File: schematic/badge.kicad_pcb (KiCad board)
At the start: 2 copper layers, 90.2 x 45.7 mm, 50 parts, among them J1 Left2, J10 Left1, J11 Penny2, J12 Penny1, J13 Penny0, J14 Power, J15 Right5, J2 Left3, J4 Serial, J5 Penny3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

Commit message: New board revision
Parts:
- removed LED1, LED10, LED2, LED3, LED4, LED5, LED6, LED7, LED8, LED9: WS2812B, LEDs:LED_WS2812B-PLCC4
- added REF***: OSHW-Logo_7.5x8mm_SilkScreen, Symbols:OSHW-Logo_7.5x8mm_SilkScreen, F.Cu at (96.9, 126.7)
- LS1: moved to B.Cu
- moved BT1 21.8 mm to (126.7, 117.6)
- moved J1 17.5 mm to (147.6, 102.2)
- moved J2 13.1 mm to (148.2, 106.4), turned to 180 degrees
- moved J14 12.7 mm to (88.2, 127.3)
- moved 1000 6.37 mm to (165.6, 107.9)
- moved 0110 6.37 mm to (121.4, 108.0)
- moved C6 6.37 mm to (119.4, 111.8)
- moved C7 6.37 mm to (110.5, 111.8)
- moved C8 6.37 mm to (101.6, 111.8)
- moved C9 6.37 mm to (92.7, 111.8)
- moved 0001 6.37 mm to (103.7, 108.0)
- moved 0010 6.37 mm to (139.2, 108.0)
- moved 0100 6.37 mm to (157.0, 108.0)
- moved 1001 6.37 mm to (94.8, 108.0)
- moved 1010 6.37 mm to (130.3, 108.0)
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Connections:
- C12 pad 1: GND -> IO2
- C13 pad 1: GND -> IO2
- J1 pad 1: IO33 -> IO34
- J4 pad 1: RX -> TX
- LS1 pad 1: IO2 -> IO13
- U1 pad 24: IO2 -> VSS
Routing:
- net IO33: track 100.3 -> 25.2 mm, vias 0 -> 2
- net IO27: track 25.7 -> 5.03 mm
- net P1: track 38.6 -> 18.3 mm
- net IO13: track 0.00 -> 19.7 mm, vias 0 -> 1
- net P3: track 59.1 -> 77.7 mm, vias 2 -> 0
- net IO32: track 1.58 -> 14.7 mm
- net IO2: track 14.9 -> 3.96 mm, vias 2 -> 1
- net IO35: track 1.71 -> 12.1 mm
- net SPI: track 22.6 -> 32.0 mm, vias 1 -> 2
- net IO34: track 1.62 -> 10.4 mm
- net RX: track 18.3 -> 10.7 mm
- net TX: track 5.83 -> 13.5 mm
- net VSS: track 91.8 -> 86.6 mm
- net VP: track 0.00 -> 3.95 mm
- net VN: track 0.00 -> 3.94 mm
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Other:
- outline, holes or cut-outs redrawn
- board text added: "+"
- board text added: "-"
- board text added: "115200 Baud"
- board text added: "Proposed BSides Iowa 2018 Badge!"
- board text added: "RX"
- board text added: "TX"
- board text added: "github.com/wrickert/badge"
- board text added: "v2"

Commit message: New board revision - power pins again
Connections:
- J14 pad 1: VDD -> VSS
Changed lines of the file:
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@@
       (net 1 VDD))
     (pad 1 thru_hole circle (at 1.905 0 90) (size 2.49936 2.49936) (drill 1.00076) (layers *.Cu *.Mask)
-      (net 1 VDD))
+      (net 2 VSS))
   )
   (module Connectors:GS2 (layer F.Cu)

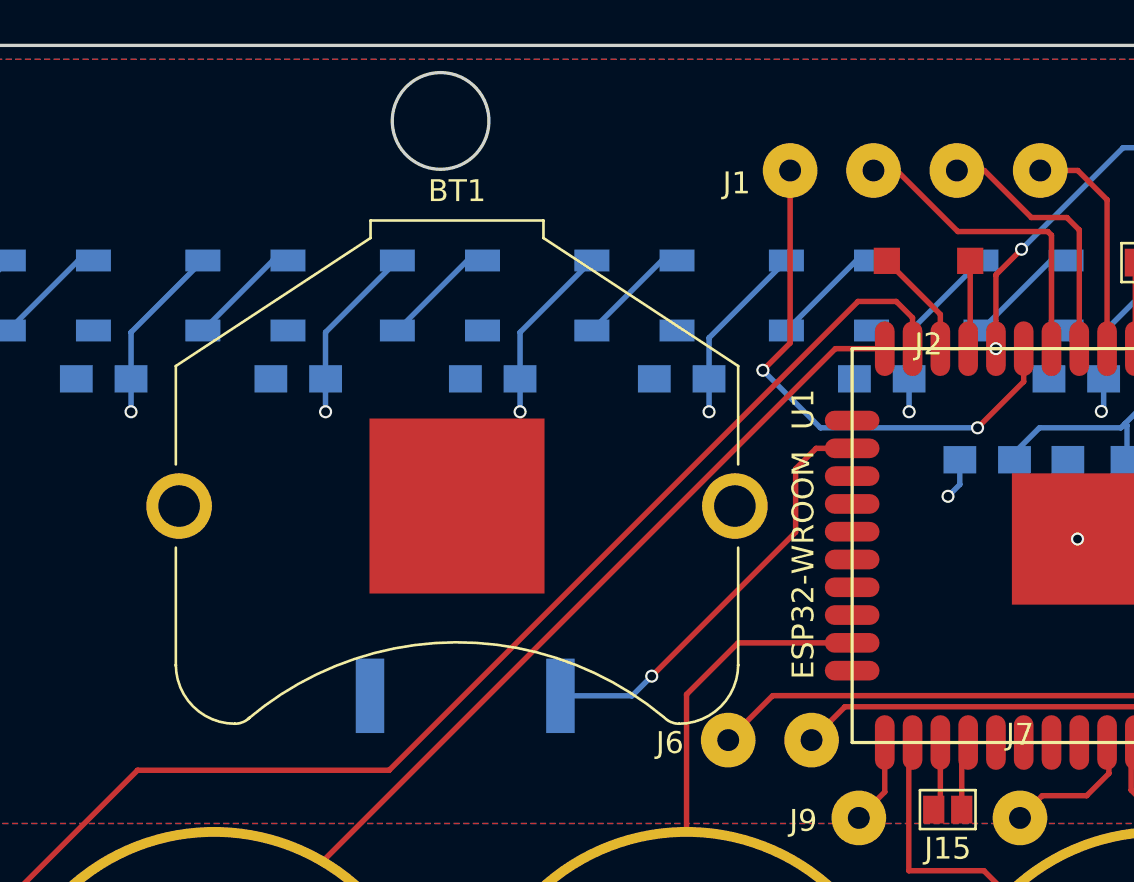
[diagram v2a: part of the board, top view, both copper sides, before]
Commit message: Fixed pizeo and power screen printing
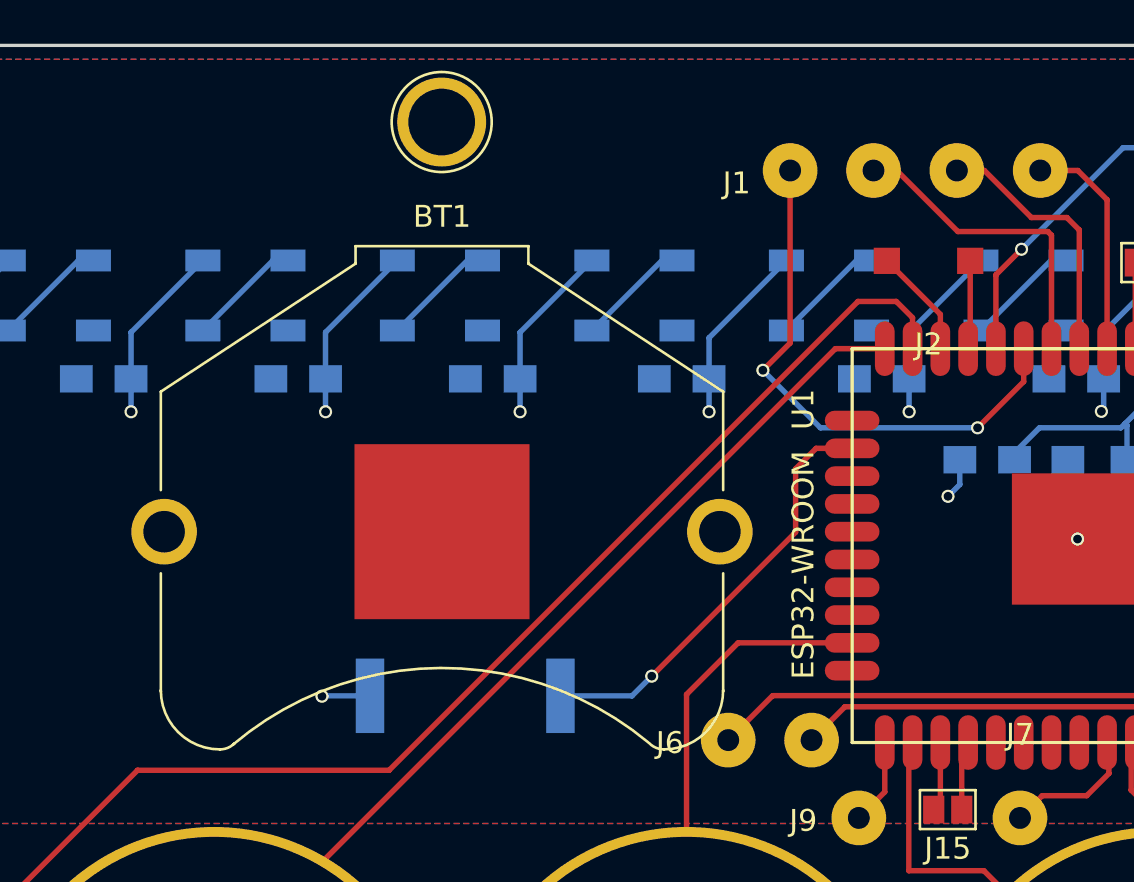
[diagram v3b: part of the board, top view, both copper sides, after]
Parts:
- added ?: 1pin, Connectors:1pin, F.Cu at (126.0, 100.0)
- moved BT1 1.36 mm to (126.0, 118.7)
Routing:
- net VSS: track 86.6 -> 88.8 mm, vias 13 -> 14
- net SPI: vias 2 -> 1
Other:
- outline, holes or cut-outs redrawn
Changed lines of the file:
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@@
   (general
     (links 88)
-    (no_connects 14)
-    (area 81.204999 96.444999 171.525001 142.315001)
+    (no_connects 53)
+    (area 81.179999 90.24 186.92 154.745)
     (thickness 1.6)
     (drawings 21)
-    (tracks 238)
+    (tracks 240)
     (zones 0)
-    (modules 41)
+    (modules 42)
     (nets 47)
   )
@@
     (31 B.Cu signal)
     (32 B.Adhes user)
-    (33 F.Adhes user)
+    (33 F.Adhes user hide)
     (34 B.Paste user)
     (35 F.Paste user)
@@
     (37 F.SilkS user)
     (38 B.Mask user)
-    (39 F.Mask user)
+    (39 F.Mask user hide)
     (40 Dwgs.User user)
     (41 Cmts.User user)
@@
     (45 Margin user)
     (46 B.CrtYd user)
-    (47 F.CrtYd user)
+    (47 F.CrtYd user hide)
     (48 B.Fab user)
-    (49 F.Fab user)
+    (49 F.Fab user hide)
   )
   (setup
@@
     (zone_45_only yes)
     (trace_min 0.2)
-    (segment_width 0.2)
+    (segment_width 0.15)
     (edge_width 0.15)
     (via_size 0.6)
@@
     (aux_axis_origin 0 0)
     (grid_origin 147.32 128.397)
-    (visible_elements FFFFF73F)
+    (visible_elements FFFFF71F)
     (pcbplotparams
       (layerselection 0x00030_80000001)
@@
   )
   (module Battery_Holders:Keystone_3009_1x2450-CoinCell (layer F.Cu)
-    (at 126.67 117.572)
+    (at 125.984 118.745)
     (descr http://www.keyelco.com/product-pdf.cfm?p=787)
     (tags "Keystone type 3009 coin cell retainer")
@@
       (xy 0.500964 -3.601424)) (layer F.SilkS) (width 0.01))
   )
+  (module Connectors:1pin (layer F.Cu)
+    (at 125.97 100.022)
+    (descr "module 1 pin (ou trou mecanique de percage)")
+    (tags DEV)
+    (fp_text reference "" (at 0.1 -4.575) (layer F.SilkS)
+      (effects (font (size 1 1) (thickness 0.15)))
+    )
+    (fp_text value 1pin (at 0 3) (layer F.Fab)
+      (effects (font (size 1 1) (thickness 0.15)))
+    )
+    (fp_circle (center 0 0) (end 2 0.8) (layer F.Fab) (width 0.1))
+    (fp_circle (center 0 0) (end 2.6 0) (layer F.CrtYd) (width 0.05))
+    (fp_circle (center 0 0) (end 0 -2.286) (layer F.SilkS) (width 0.12))
+    (pad 1 thru_hole circle (at 0 0) (size 4.064 4.064) (drill 3.048) (layers *.Cu *.Mask))
+  )
   (gr_text "v2\n" (at 83.99 98.847) (layer F.SilkS)
     (effects (font (size 1.5 1.5) (thickness 0.3)))
@@
     (effects (font (size 1.5 1.5) (thickness 0.3) italic) (justify mirror))
   )
-  (gr_circle (center 125.92 99.972) (end 126.12 102.172) (layer Edge.Cuts) (width 0.15))
+  (gr_circle (center 125.92 99.972) (end 126.12 102.172) (layer B.Fab) (width 0.15))
   (gr_text "Proposed BSides Iowa 2018 Badge!" (at 149.545 99.822) (layer B.SilkS)
     (effects (font (size 1.5 1.5) (thickness 0.3)) (justify mirror))
   )
-  (gr_text - (at 90.805 129.032) (layer B.SilkS)
+  (gr_text + (at 90.805 129.032) (layer B.SilkS)
     (effects (font (size 1.5 1.5) (thickness 0.3)) (justify mirror))
   )
-  (gr_text "+\n" (at 90.805 125.222) (layer B.SilkS)
+  (gr_text "-\n" (at 90.805 125.222) (layer B.SilkS)
     (effects (font (size 1.5 1.5) (thickness 0.3)) (justify mirror))
   )
@@
   (segment (start 145.615 109.55) (end 145.575 109.51) (width 0.25) (layer B.Cu) (net 1))
   (segment (start 154.505 109.55) (end 154.465 109.51) (width 0.25) (layer B.Cu) (net 1))
+  (segment (start 122.695 126.247) (end 120.514 126.247) (width 0.25) (layer B.Cu) (net 2) (status 400000))
+  (via (at 120.4976 126.2634) (size 0.6) (drill 0.4) (layers F.Cu B.Cu) (net 2))
+  (segment (start 120.514 126.247) (end 120.4976 126.2634) (width 0.25) (layer B.Cu) (net 2))
   (segment (start 168.095 106.322) (end 168.095 105.932) (width 0.25) (layer B.Cu) (net 2))
   (segment (start 168.095 105.932) (end 165.8 103.637) (width 0.25) (layer B.Cu) (net 2))
@@
   (segment (start 169.79 107.147) (end 169.79 104.187) (width 0.25) (layer B.Cu) (net 3))
   (segment (start 168.095 108.842) (end 169.79 107.147) (width 0.25) (layer B.Cu) (net 3))
-  (via (at 151.3 110.38) (size 0.6) (drill 0.4) (layers F.Cu B.Cu) (net 3))
   (segment (start 168.689 109.844) (end 168.395 109.55) (width 0.25) (layer B.Cu) (net 3))
   (segment (start 163.395 106.35) (end 162.705 106.35) (width 0.25) (layer B.Cu) (net 4))
@@
   (segment (start 150.125 106.367) (end 150.125 110.285) (width 0.25) (layer F.Cu) (net 38))
   (segment (start 150.125 110.285) (end 150.03 110.38) (width 0.25) (layer F.Cu) (net 38))
-  (segment (start 141.895 102.237) (end 141.895 110.122) (width 0.25) (layer F.Cu) (net 39) (status 400000))
-  (segment (start 152.57 111.887) (end 152.57 110.38) (width 0.25) (layer F.Cu) (net 39) (status 800000))
+  (segment (start 141.895 102.237) (end 141.895 110.122) (width 0.25) (layer F.Cu) (net 39))
+  (segment (start 152.57 111.887) (end 152.57 110.38) (width 0.25) (layer F.Cu) (net 39))
   (segment (start 150.46 113.997) (end 152.57 111.887) (width 0.25) (layer F.Cu) (net 39))
   (via (at 150.46 113.997) (size 0.6) (drill 0.4) (layers F.Cu B.Cu) (net 39))
@@
   (segment (start 141.895 110.122) (end 140.65 111.367) (width 0.25) (layer F.Cu) (net 39))
   (segment (start 152.654 110.296) (end 152.57 110.38) (width 0.25) (layer F.Cu) (net 39))
-  (segment (start 145.705 102.237) (end 146.77 102.237) (width 0.25) (layer F.Cu) (net 40) (status C00000))
-  (segment (start 146.77 102.237) (end 149.56 105.027) (width 0.25) (layer F.Cu) (net 40) (status 400000))
+  (segment (start 145.705 102.237) (end 146.77 102.237) (width 0.25) (layer F.Cu) (net 40))
+  (segment (start 146.77 102.237) (end 149.56 105.027) (width 0.25) (layer F.Cu) (net 40))
   (segment (start 149.56 105.027) (end 153.67 105.027) (width 0.25) (layer F.Cu) (net 40))
   (segment (start 153.67 105.027) (end 153.84 105.197) (width 0.25) (layer F.Cu) (net 40))
-  (segment (start 153.84 105.197) (end 153.84 110.38) (width 0.25) (layer F.Cu) (net 40) (status 800000))
+  (segment (start 153.84 105.197) (end 153.84 110.38) (width 0.25) (layer F.Cu) (net 40))
   (segment (start 153.924 110.296) (end 153.84 110.38) (width 0.25) (layer F.Cu) (net 40))
-  (segment (start 149.515 102.237) (end 150.77 102.237) (width 0.25) (layer F.Cu) (net 41) (status 400000))
-  (segment (start 155.11 104.957) (end 155.11 110.38) (width 0.25) (layer F.Cu) (net 41) (status 800000))
+  (segment (start 149.515 102.237) (end 150.77 102.237) (width 0.25) (layer F.Cu) (net 41))
+  (segment (start 155.11 104.957) (end 155.11 110.38) (width 0.25) (layer F.Cu) (net 41))
   (segment (start 154.54 104.387) (end 155.11 104.957) (width 0.25) (layer F.Cu) (net 41))
   (segment (start 152.92 104.387) (end 154.54 104.387) (width 0.25) (layer F.Cu) (net 41))
   (segment (start 150.77 102.237) (end 152.92 104.387) (width 0.25) (layer F.Cu) (net 41))
-  (segment (start 153.325 102.237) (end 155.04 102.237) (width 0.25) (layer F.Cu) (net 42) (status 400000))
-  (segment (start 156.38 103.577) (end 156.38 110.38) (width 0.25) (layer F.Cu) (net 42) (status 800000))
+  (segment (start 153.325 102.237) (end 155.04 102.237) (width 0.25) (layer F.Cu) (net 42))
+  (segment (start 156.38 103.577) (end 156.38 110.38) (width 0.25) (layer F.Cu) (net 42))
   (segment (start 155.04 102.237) (end 156.38 103.577) (width 0.25) (layer F.Cu) (net 42))
   (segment (start 157.67 106.447) (end 157.67 110.36) (width 0.25) (layer F.Cu) (net 43))
@@
     (connect_pads (clearance 0.508))
     (min_thickness 0.254)
-    (fill yes (arc_segments 16) (thermal_gap 0.508) (thermal_bridge_width 0.508))
+    (fill (arc_segments 16) (thermal_gap 0.508) (thermal_bridge_width 0.508))
     (polygon
       (pts
@@
     (connect_pads (clearance 0.508))
     (min_thickness 0.254)
-    (fill yes (arc_segments 16) (thermal_gap 0.508) (thermal_bridge_width 0.508))
+    (fill (arc_segments 16) (thermal_gap 0.508) (thermal_bridge_width 0.508))
     (polygon
       (pts

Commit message: vallen says hi
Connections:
- C12 pad 1: IO2 -> VSS
- C13 pad 1: IO2 -> VSS
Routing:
- net IO2: track 3.96 -> 0.00 mm, vias 1 -> 0
- net VSS: track 88.8 -> 92.7 mm, vias 14 -> 15
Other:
- board text added: "WR"
